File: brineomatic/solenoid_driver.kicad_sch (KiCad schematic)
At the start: 8 parts, among them J5 3.5MM, J6 3.5MM, Q1 AO3400A

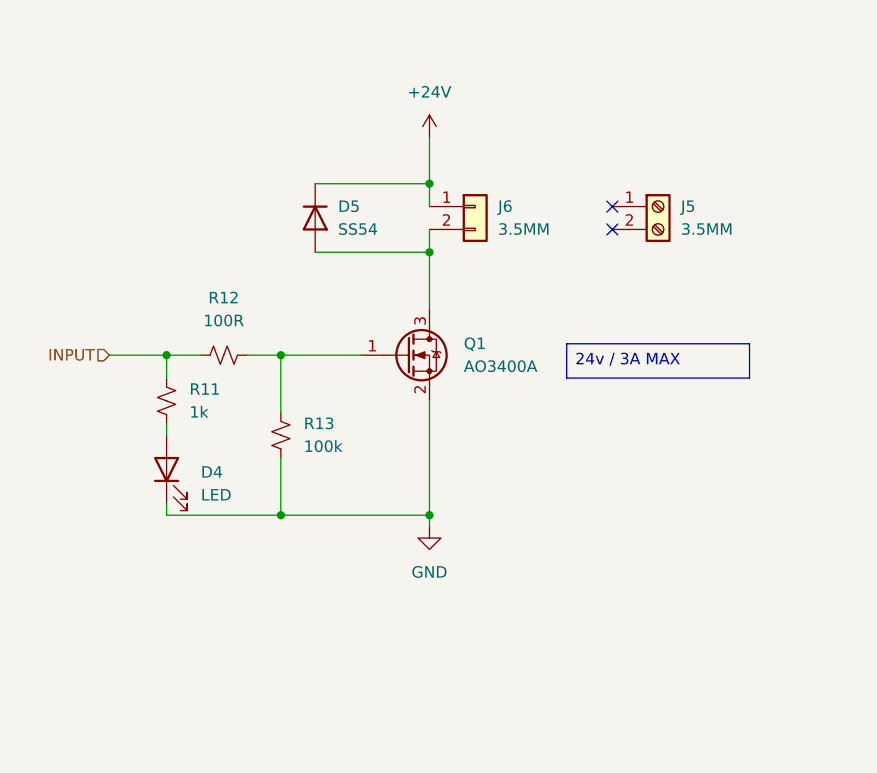
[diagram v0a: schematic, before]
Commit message: tmc2209 driver schematic checked and laid out nicely.
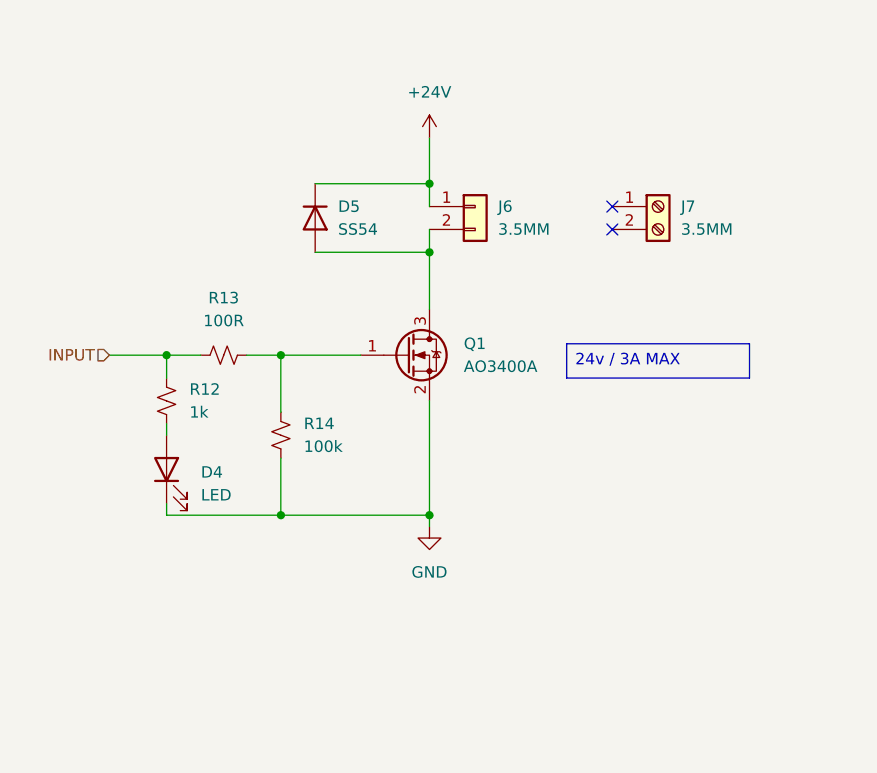
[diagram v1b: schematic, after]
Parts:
- renumbered J5 to J7, R11 to R12, R12 to R13, R13 to R14
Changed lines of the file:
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@@
 			(project "brineomatic"
 				(path "/96477ae2-ef08-48f3-8dd4-fe4478541f68/427089b2-03f8-442f-beb9-df87f2c31083"
-					(reference "D15")
+					(reference "D16")
 					(unit 1)
 				)
@@
 				)
 				(path "/96477ae2-ef08-48f3-8dd4-fe4478541f68/c855463c-7233-4758-aee4-aa81e2b08bc2"
-					(reference "D13")
-					(unit 1)
-				)
-				(path "/96477ae2-ef08-48f3-8dd4-fe4478541f68/dbb171ac-9e75-41dd-9596-6fac72a797a4"
-					(reference "D17")
+					(reference "D14")
+					(unit 1)
+				)
+				(path "/96477ae2-ef08-48f3-8dd4-fe4478541f68/dbb171ac-9e75-41dd-9596-6fac72a797a4"
+					(reference "D18")
 					(unit 1)
 				)
@@
 		(dnp no)
 		(fields_autoplaced yes)
-		(property "Reference" "J5"
+		(property "Reference" "J7"
 			(at 166.37 72.3899 0)
 			(effects
@@
 			(project ""
 				(path "/96477ae2-ef08-48f3-8dd4-fe4478541f68/427089b2-03f8-442f-beb9-df87f2c31083"
+					(reference "J14")
+					(unit 1)
+				)
+				(path "/96477ae2-ef08-48f3-8dd4-fe4478541f68/91db2587-0f96-4292-982e-c9eb44a28398"
+					(reference "J7")
+					(unit 1)
+				)
+				(path "/96477ae2-ef08-48f3-8dd4-fe4478541f68/c855463c-7233-4758-aee4-aa81e2b08bc2"
+					(reference "J12")
+					(unit 1)
+				)
+				(path "/96477ae2-ef08-48f3-8dd4-fe4478541f68/dbb171ac-9e75-41dd-9596-6fac72a797a4"
 					(reference "J16")
-					(unit 1)
-				)
-				(path "/96477ae2-ef08-48f3-8dd4-fe4478541f68/91db2587-0f96-4292-982e-c9eb44a28398"
-					(reference "J5")
-					(unit 1)
-				)
-				(path "/96477ae2-ef08-48f3-8dd4-fe4478541f68/c855463c-7233-4758-aee4-aa81e2b08bc2"
-					(reference "J13")
-					(unit 1)
-				)
-				(path "/96477ae2-ef08-48f3-8dd4-fe4478541f68/dbb171ac-9e75-41dd-9596-6fac72a797a4"
-					(reference "J17")
 					(unit 1)
 				)
@@
 		(dnp no)
 		(fields_autoplaced yes)
-		(property "Reference" "#PWR019"
+		(property "Reference" "#PWR020"
 			(at 138.43 114.3 0)
 			(effects
@@
 			(project "brineomatic"
 				(path "/96477ae2-ef08-48f3-8dd4-fe4478541f68/427089b2-03f8-442f-beb9-df87f2c31083"
-					(reference "#PWR032")
-					(unit 1)
-				)
-				(path "/96477ae2-ef08-48f3-8dd4-fe4478541f68/91db2587-0f96-4292-982e-c9eb44a28398"
-					(reference "#PWR019")
-					(unit 1)
-				)
-				(path "/96477ae2-ef08-48f3-8dd4-fe4478541f68/c855463c-7233-4758-aee4-aa81e2b08bc2"
-					(reference "#PWR030")
-					(unit 1)
-				)
-				(path "/96477ae2-ef08-48f3-8dd4-fe4478541f68/dbb171ac-9e75-41dd-9596-6fac72a797a4"
+					(reference "#PWR036")
+					(unit 1)
+				)
+				(path "/96477ae2-ef08-48f3-8dd4-fe4478541f68/91db2587-0f96-4292-982e-c9eb44a28398"
+					(reference "#PWR020")
+					(unit 1)
+				)
+				(path "/96477ae2-ef08-48f3-8dd4-fe4478541f68/c855463c-7233-4758-aee4-aa81e2b08bc2"
 					(reference "#PWR034")
+					(unit 1)
+				)
+				(path "/96477ae2-ef08-48f3-8dd4-fe4478541f68/dbb171ac-9e75-41dd-9596-6fac72a797a4"
+					(reference "#PWR038")
 					(unit 1)
 				)
@@
 		(dnp no)
 		(fields_autoplaced yes)
-		(property "Reference" "R11"
+		(property "Reference" "R12"
 			(at 111.76 92.7099 0)
 			(effects
@@
 			(project "brineomatic"
 				(path "/96477ae2-ef08-48f3-8dd4-fe4478541f68/427089b2-03f8-442f-beb9-df87f2c31083"
-					(reference "R25")
-					(unit 1)
-				)
-				(path "/96477ae2-ef08-48f3-8dd4-fe4478541f68/91db2587-0f96-4292-982e-c9eb44a28398"
-					(reference "R11")
-					(unit 1)
-				)
-				(path "/96477ae2-ef08-48f3-8dd4-fe4478541f68/c855463c-7233-4758-aee4-aa81e2b08bc2"
-					(reference "R22")
-					(unit 1)
-				)
-				(path "/96477ae2-ef08-48f3-8dd4-fe4478541f68/dbb171ac-9e75-41dd-9596-6fac72a797a4"
-					(reference "R28")
+					(reference "R27")
+					(unit 1)
+				)
+				(path "/96477ae2-ef08-48f3-8dd4-fe4478541f68/91db2587-0f96-4292-982e-c9eb44a28398"
+					(reference "R12")
+					(unit 1)
+				)
+				(path "/96477ae2-ef08-48f3-8dd4-fe4478541f68/c855463c-7233-4758-aee4-aa81e2b08bc2"
+					(reference "R24")
+					(unit 1)
+				)
+				(path "/96477ae2-ef08-48f3-8dd4-fe4478541f68/dbb171ac-9e75-41dd-9596-6fac72a797a4"
+					(reference "R30")
 					(unit 1)
 				)
@@
 		(dnp no)
 		(fields_autoplaced yes)
-		(property "Reference" "R12"
+		(property "Reference" "R13"
 			(at 115.57 82.55 90)
 			(effects
@@
 			(project "brineomatic"
 				(path "/96477ae2-ef08-48f3-8dd4-fe4478541f68/427089b2-03f8-442f-beb9-df87f2c31083"
-					(reference "R26")
-					(unit 1)
-				)
-				(path "/96477ae2-ef08-48f3-8dd4-fe4478541f68/91db2587-0f96-4292-982e-c9eb44a28398"
-					(reference "R12")
-					(unit 1)
-				)
-				(path "/96477ae2-ef08-48f3-8dd4-fe4478541f68/c855463c-7233-4758-aee4-aa81e2b08bc2"
-					(reference "R23")
-					(unit 1)
-				)
-				(path "/96477ae2-ef08-48f3-8dd4-fe4478541f68/dbb171ac-9e75-41dd-9596-6fac72a797a4"
-					(reference "R29")
+					(reference "R28")
+					(unit 1)
+				)
+				(path "/96477ae2-ef08-48f3-8dd4-fe4478541f68/91db2587-0f96-4292-982e-c9eb44a28398"
+					(reference "R13")
+					(unit 1)
+				)
+				(path "/96477ae2-ef08-48f3-8dd4-fe4478541f68/c855463c-7233-4758-aee4-aa81e2b08bc2"
+					(reference "R25")
+					(unit 1)
+				)
+				(path "/96477ae2-ef08-48f3-8dd4-fe4478541f68/dbb171ac-9e75-41dd-9596-6fac72a797a4"
+					(reference "R31")
 					(unit 1)
 				)
@@
 			(project "brineomatic"
 				(path "/96477ae2-ef08-48f3-8dd4-fe4478541f68/427089b2-03f8-442f-beb9-df87f2c31083"
-					(reference "J10")
+					(reference "J13")
 					(unit 1)
 				)
@@
 				)
 				(path "/96477ae2-ef08-48f3-8dd4-fe4478541f68/c855463c-7233-4758-aee4-aa81e2b08bc2"
-					(reference "J9")
-					(unit 1)
-				)
-				(path "/96477ae2-ef08-48f3-8dd4-fe4478541f68/dbb171ac-9e75-41dd-9596-6fac72a797a4"
 					(reference "J11")
+					(unit 1)
+				)
+				(path "/96477ae2-ef08-48f3-8dd4-fe4478541f68/dbb171ac-9e75-41dd-9596-6fac72a797a4"
+					(reference "J15")
 					(unit 1)
 				)
@@
 		(dnp no)
 		(fields_autoplaced yes)
-		(property "Reference" "R13"
+		(property "Reference" "R14"
 			(at 124.46 96.5199 0)
 			(effects
@@
 			(project "brineomatic"
 				(path "/96477ae2-ef08-48f3-8dd4-fe4478541f68/427089b2-03f8-442f-beb9-df87f2c31083"
-					(reference "R27")
-					(unit 1)
-				)
-				(path "/96477ae2-ef08-48f3-8dd4-fe4478541f68/91db2587-0f96-4292-982e-c9eb44a28398"
-					(reference "R13")
-					(unit 1)
-				)
-				(path "/96477ae2-ef08-48f3-8dd4-fe4478541f68/c855463c-7233-4758-aee4-aa81e2b08bc2"
-					(reference "R24")
-					(unit 1)
-				)
-				(path "/96477ae2-ef08-48f3-8dd4-fe4478541f68/dbb171ac-9e75-41dd-9596-6fac72a797a4"
-					(reference "R30")
+					(reference "R29")
+					(unit 1)
+				)
+				(path "/96477ae2-ef08-48f3-8dd4-fe4478541f68/91db2587-0f96-4292-982e-c9eb44a28398"
+					(reference "R14")
+					(unit 1)
+				)
+				(path "/96477ae2-ef08-48f3-8dd4-fe4478541f68/c855463c-7233-4758-aee4-aa81e2b08bc2"
+					(reference "R26")
+					(unit 1)
+				)
+				(path "/96477ae2-ef08-48f3-8dd4-fe4478541f68/dbb171ac-9e75-41dd-9596-6fac72a797a4"
+					(reference "R32")
 					(unit 1)
 				)
@@
 			(project "brineomatic"
 				(path "/96477ae2-ef08-48f3-8dd4-fe4478541f68/427089b2-03f8-442f-beb9-df87f2c31083"
+					(reference "Q5")
+					(unit 1)
+				)
+				(path "/96477ae2-ef08-48f3-8dd4-fe4478541f68/91db2587-0f96-4292-982e-c9eb44a28398"
+					(reference "Q1")
+					(unit 1)
+				)
+				(path "/96477ae2-ef08-48f3-8dd4-fe4478541f68/c855463c-7233-4758-aee4-aa81e2b08bc2"
 					(reference "Q4")
 					(unit 1)
 				)
-				(path "/96477ae2-ef08-48f3-8dd4-fe4478541f68/91db2587-0f96-4292-982e-c9eb44a28398"
-					(reference "Q1")
-					(unit 1)
-				)
-				(path "/96477ae2-ef08-48f3-8dd4-fe4478541f68/c855463c-7233-4758-aee4-aa81e2b08bc2"
-					(reference "Q3")
-					(unit 1)
-				)
-				(path "/96477ae2-ef08-48f3-8dd4-fe4478541f68/dbb171ac-9e75-41dd-9596-6fac72a797a4"
-					(reference "Q5")
+				(path "/96477ae2-ef08-48f3-8dd4-fe4478541f68/dbb171ac-9e75-41dd-9596-6fac72a797a4"
+					(reference "Q6")
 					(unit 1)
 				)
@@
 		(dnp no)
 		(fields_autoplaced yes)
-		(property "Reference" "#PWR018"
+		(property "Reference" "#PWR019"
 			(at 138.43 68.58 0)
 			(effects
@@
 			(project "brineomatic"
 				(path "/96477ae2-ef08-48f3-8dd4-fe4478541f68/427089b2-03f8-442f-beb9-df87f2c31083"
-					(reference "#PWR031")
-					(unit 1)
-				)
-				(path "/96477ae2-ef08-48f3-8dd4-fe4478541f68/91db2587-0f96-4292-982e-c9eb44a28398"
-					(reference "#PWR018")
-					(unit 1)
-				)
-				(path "/96477ae2-ef08-48f3-8dd4-fe4478541f68/c855463c-7233-4758-aee4-aa81e2b08bc2"
-					(reference "#PWR029")
-					(unit 1)
-				)
-				(path "/96477ae2-ef08-48f3-8dd4-fe4478541f68/dbb171ac-9e75-41dd-9596-6fac72a797a4"
+					(reference "#PWR035")
+					(unit 1)
+				)
+				(path "/96477ae2-ef08-48f3-8dd4-fe4478541f68/91db2587-0f96-4292-982e-c9eb44a28398"
+					(reference "#PWR019")
+					(unit 1)
+				)
+				(path "/96477ae2-ef08-48f3-8dd4-fe4478541f68/c855463c-7233-4758-aee4-aa81e2b08bc2"
 					(reference "#PWR033")
+					(unit 1)
+				)
+				(path "/96477ae2-ef08-48f3-8dd4-fe4478541f68/dbb171ac-9e75-41dd-9596-6fac72a797a4"
+					(reference "#PWR037")
 					(unit 1)
 				)
@@
 			(project "brineomatic"
 				(path "/96477ae2-ef08-48f3-8dd4-fe4478541f68/427089b2-03f8-442f-beb9-df87f2c31083"
-					(reference "D14")
+					(reference "D15")
 					(unit 1)
 				)
@@
 				)
 				(path "/96477ae2-ef08-48f3-8dd4-fe4478541f68/c855463c-7233-4758-aee4-aa81e2b08bc2"
-					(reference "D12")
-					(unit 1)
-				)
-				(path "/96477ae2-ef08-48f3-8dd4-fe4478541f68/dbb171ac-9e75-41dd-9596-6fac72a797a4"
-					(reference "D16")
-					(unit 1)
-				)
+					(reference "D13")
+					(unit 1)
+				)
+				(path "/96477ae2-ef08-48f3-8dd4-fe4478541f68/dbb171ac-9e75-41dd-9596-6fac72a797a4"
+					(reference "D17")
+					(unit 1)
+				)

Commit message: fully routed and erc/drc passed
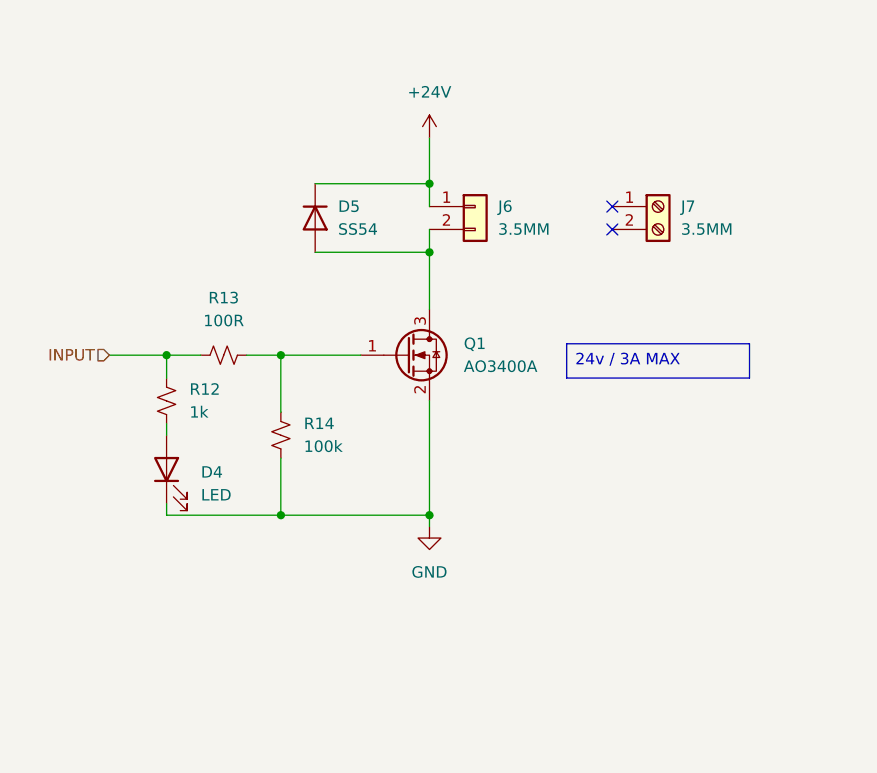
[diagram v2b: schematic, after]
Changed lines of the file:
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@@
+			)
+		)
+		(property "Sim.Pins" "1=K 2=A"
+			(at 109.22 101.6 0)
+			(effects
+				(font
+					(size 1.27 1.27)
+				)
+				(hide yes)
 			)
 		)

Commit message: silkscreen good and all drc errors fixed.
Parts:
- J6: footprint Connector_Phoenix_MC:PhoenixContact_MC_1,5_2-G-3.5_1x02_P3.50mm_Horizontal -> yarrboard:PhoenixContact_MC_1,5_2-G-3.5_1x02_P3.50mm_Horizontal
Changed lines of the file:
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@@
 			)
 		)
-		(property "Footprint" "Connector_Phoenix_MC:PhoenixContact_MC_1,5_2-G-3.5_1x02_P3.50mm_Horizontal"
+		(property "Footprint" "yarrboard:PhoenixContact_MC_1,5_2-G-3.5_1x02_P3.50mm_Horizontal"
 			(at 143.51 72.39 0)
 			(effects

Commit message: worked on bom for rev b prototype run
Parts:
- D4: value LED -> RED; LCSC C98224 -> C965799
- R12: LCSC C95781 -> (none)
- R13: LCSC C105577 -> (none)
- R14: LCSC C96346 -> (none)
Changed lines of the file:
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@@
 			)
 		)
-		(property "LCSC" "C95781"
+		(property "LCSC" ""
 			(at 109.22 93.98 0)
 			(effects
@@
 			)
 		)
-		(property "LCSC" "C105577"
+		(property "LCSC" ""
 			(at 115.57 88.9 0)
 			(effects
@@
 			)
 		)
-		(property "LCSC" "C96346"
+		(property "LCSC" ""
 			(at 121.92 97.79 0)
 			(effects
@@
 			)
 		)
-		(property "Value" "LED"
+		(property "Value" "RED"
 			(at 113.03 104.4574 90)
 			(effects
@@
 			)
 		)
-		(property "LCSC" "C98224"
+		(property "LCSC" "C965799"
 			(at 109.22 101.6 0)
 			(effects

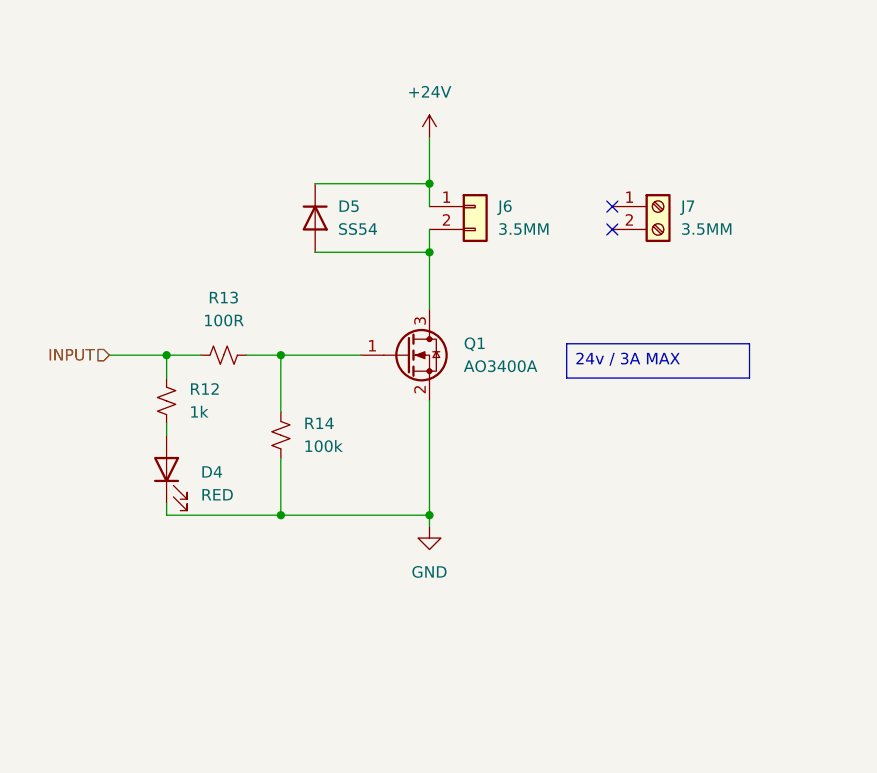
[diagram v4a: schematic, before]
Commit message: added qwiic i2c connector
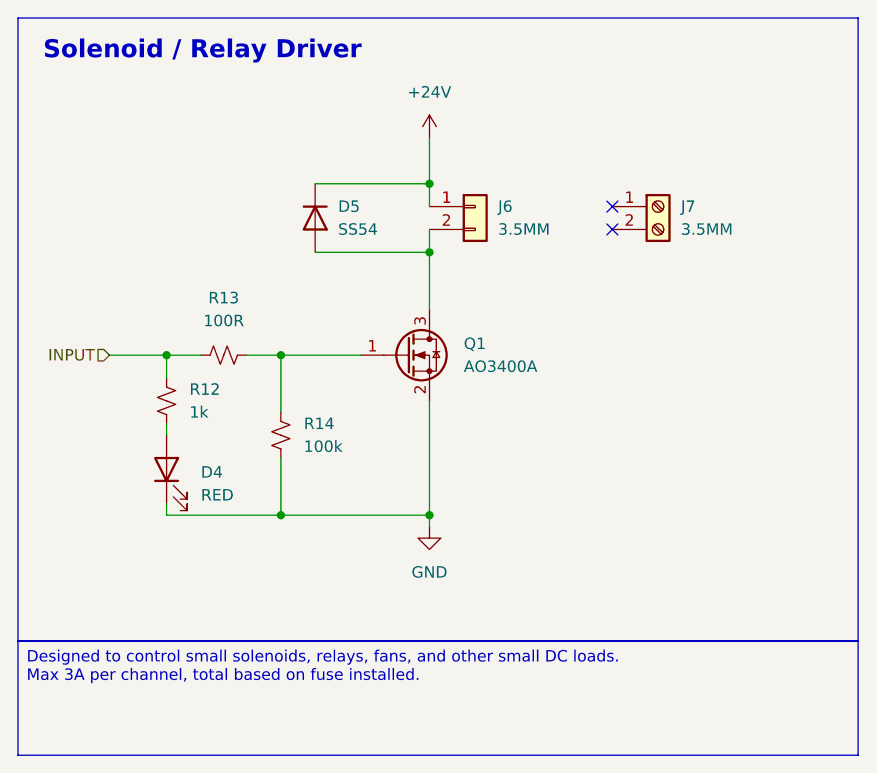
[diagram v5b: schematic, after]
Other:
- note added: "Solenoid / Relay Driver"
- title: (none) -> https://github.com/hoeken/brineomatic
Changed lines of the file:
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@@
 	(generator_version "9.0")
 	(paper "A4")
-	(text_box "24v / 3A MAX"
-		(exclude_from_sim no)
-		(at 153.67 87.63 0)
-		(size 20.32 3.81)
-		(margins 0.9525 0.9525 0.9525 0.9525)
+	(title_block
+		(title "https://github.com/hoeken/brineomatic")
+		(date "2025-08-28")
+		(rev "B")
+	)
+	(rectangle
+		(start 92.71 51.435)
+		(end 186.055 120.65)
 		(stroke
 			(width 0)
@@
 		)
 		(fill
+			(type none)
+		)
+	)
+	(text "Solenoid / Relay Driver"
+		(exclude_from_sim no)
+		(at 95.504 55.118 0)
+		(effects
+			(font
+				(size 2 2)
+				(thickness 0.4)
+				(bold yes)
+			)
+			(justify left)
+		)
+	)
+	(text_box "Designed to control small solenoids, relays, fans, and other small DC loads.\nMax 3A per channel, total based on fuse installed."
+		(exclude_from_sim no)
+		(at 92.71 120.65 0)
+		(size 93.345 12.7)
+		(margins 0.9525 0.9525 0.9525 0.9525)
+		(stroke
+			(width 0)
+			(type solid)
+		)
+		(fill
